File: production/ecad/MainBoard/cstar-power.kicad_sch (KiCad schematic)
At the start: 32 parts, among them IC1 LT8648SEV#PBF, U1 AZ1117IH-3.3TRG1

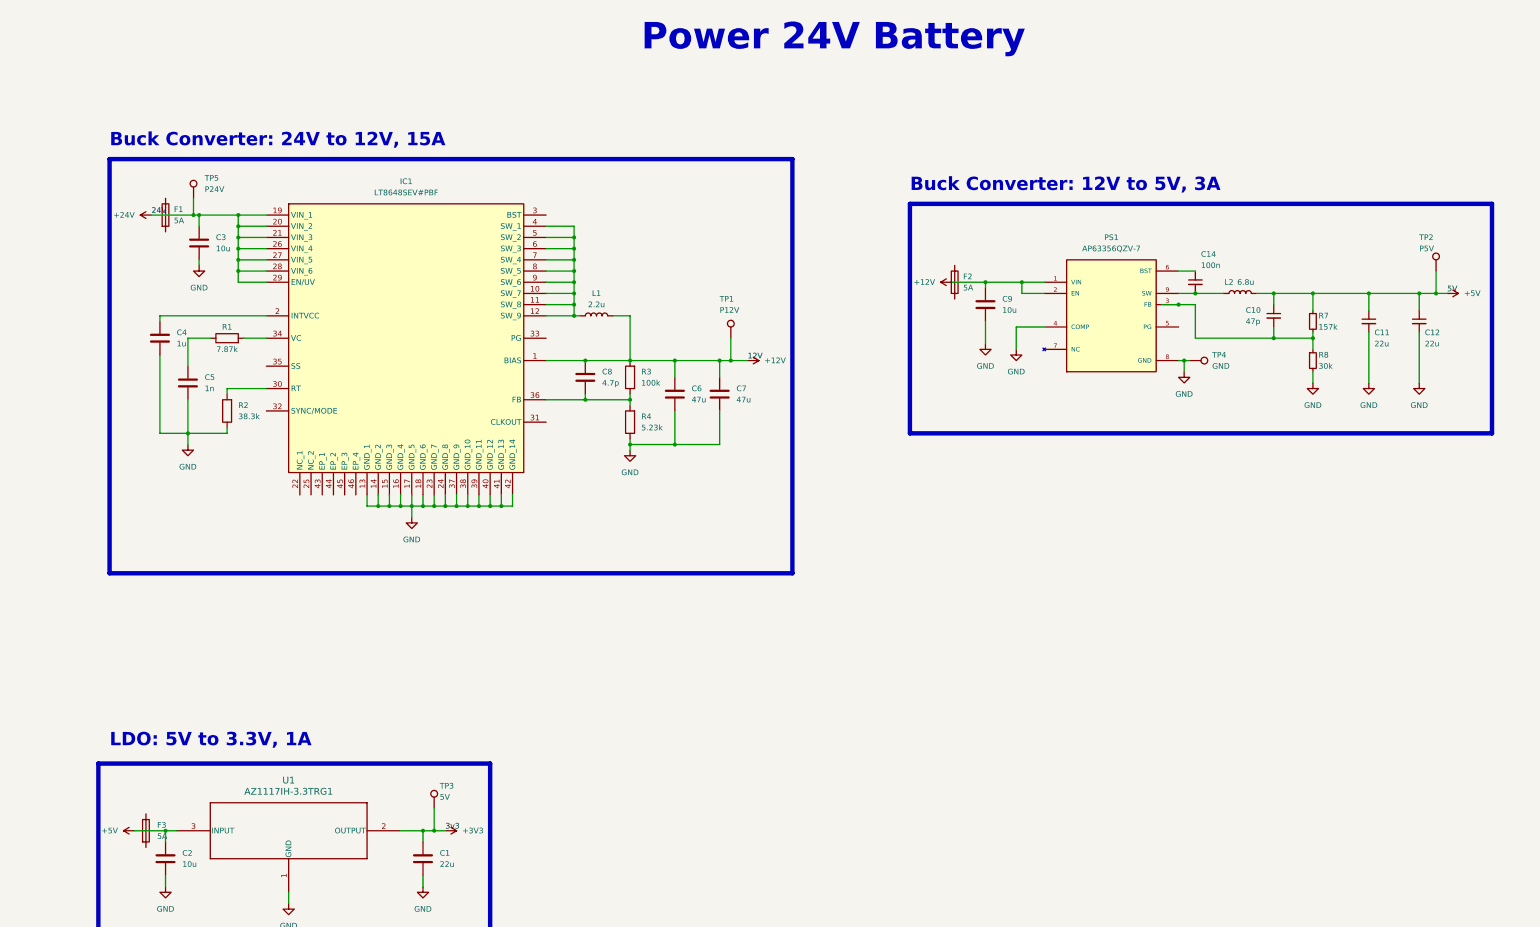
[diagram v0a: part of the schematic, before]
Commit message: Fuses position was fixed
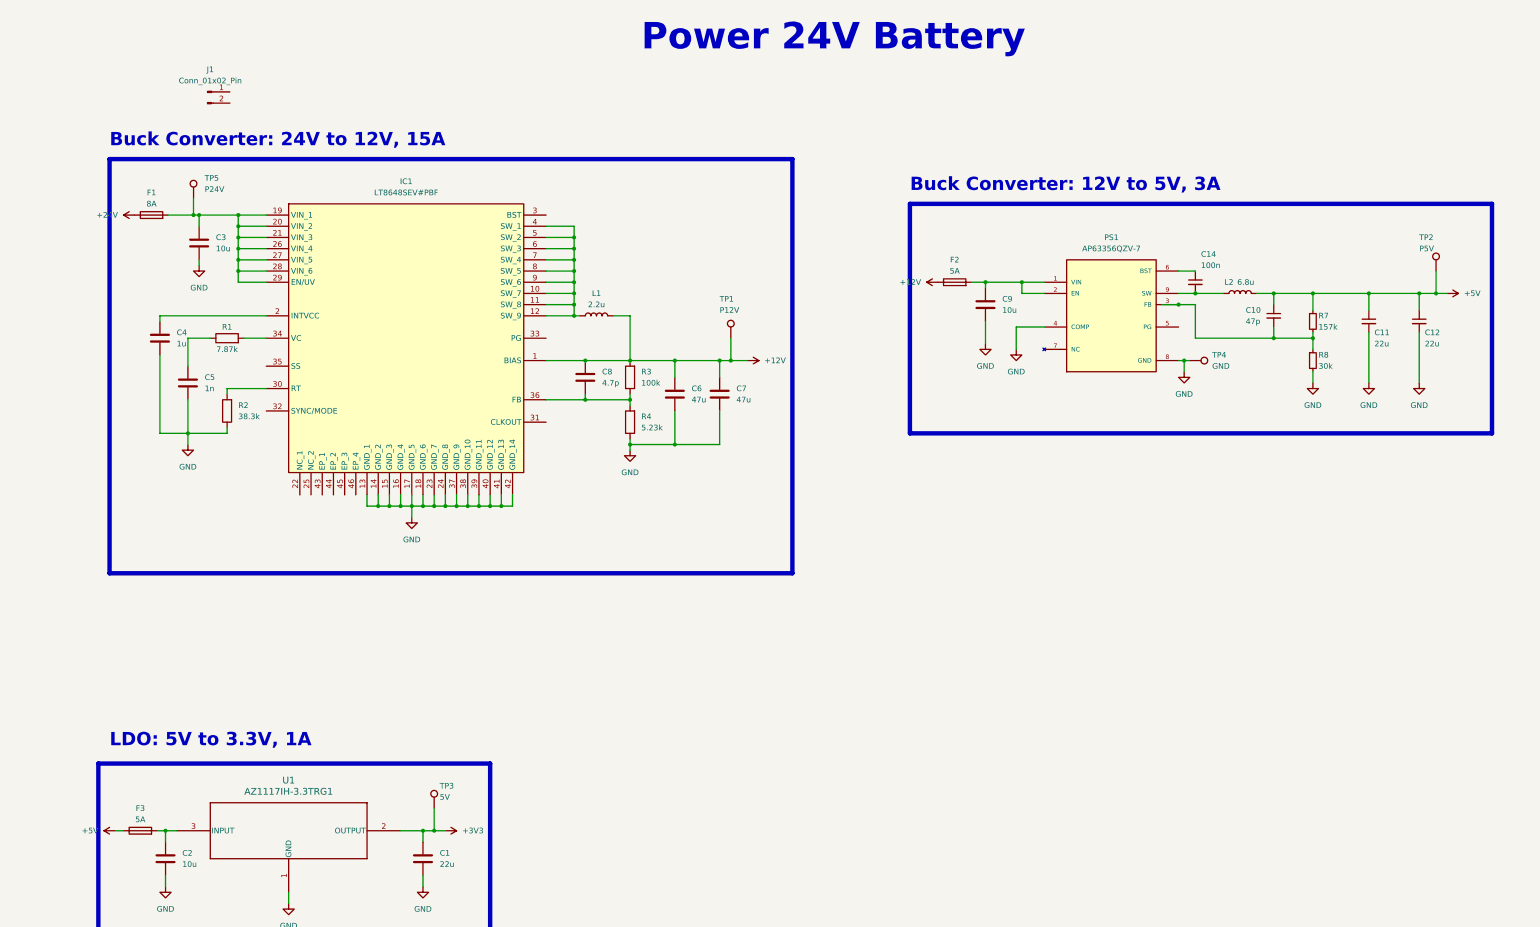
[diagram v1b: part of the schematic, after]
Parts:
- added J1: Conn_01x02_Pin, symbol Connector:Conn_01x02_Pin
- F1: value 5A -> 8A
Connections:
- net +12V: now also F2.1; no longer C9.1, PS1.1 (VIN), PS1.2 (EN)
- net +24V: now also F1.1; no longer C3.1, IC1.19 (VIN_1), IC1.20 (VIN_2), IC1.21 (VIN_3), IC1.26 (VIN_4), IC1.27 (VIN_5), IC1.28 (VIN_6), IC1.29 (EN/UV), TP5.1
- net +5V: now also F3.1; no longer C2.1, U1.3 (INPUT)
- net at F2.2: now also C9.1, PS1.1 (VIN), PS1.2 (EN)
- net at F1.2: now also C3.1, IC1.19 (VIN_1), IC1.20 (VIN_2), IC1.21 (VIN_3), IC1.26 (VIN_4), IC1.27 (VIN_5), IC1.28 (VIN_6), IC1.29 (EN/UV), TP5.1
- net at F3.2: now also C2.1, U1.3 (INPUT)
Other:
- moved on the sheet: F1, F2, F3
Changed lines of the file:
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@@
+    (stroke (width 0) (type default))
+  )
+  (wire (pts (xy 51.435 204.47) (xy 53.34 204.47))
     (stroke (width 0) (type default))
   )
@@
     (stroke (width 0) (type default))
   )
-  (wire (pts (xy 231.775 80.01) (xy 239.395 80.01))
-    (stroke (width 0) (type default))
-  )
   (wire (pts (xy 139.7 80.01) (xy 146.05 80.01))
     (stroke (width 0) (type default))
@@
     (stroke (width 0) (type default))
   )
+  (wire (pts (xy 53.975 64.77) (xy 59.69 64.77))
+    (stroke (width 0) (type default))
+  )
   (wire (pts (xy 111.76 204.47) (xy 114.3 204.47))
     (stroke (width 0) (type default))
@@
     (stroke (width 0) (type default))
   )
-  (wire (pts (xy 50.165 64.77) (xy 59.69 64.77))
-    (stroke (width 0) (type default))
-  )
   (wire (pts (xy 58.42 106.68) (xy 58.42 114.3))
     (stroke (width 0) (type default))
@@
     (stroke (width 0) (type default))
   )
-  (wire (pts (xy 46.355 204.47) (xy 53.34 204.47))
+  (wire (pts (xy 236.22 80.01) (xy 239.395 80.01))
+    (stroke (width 0) (type default))
+  )
+  (wire (pts (xy 41.91 204.47) (xy 43.815 204.47))
     (stroke (width 0) (type default))
   )
@@
     (effects (font (size 3 3) (thickness 0.6) bold) (justify left bottom))
   )
-  (label "3v3" (at 116.84 204.47 0) (fields_autoplaced)
-    (effects (font (size 1.27 1.27)) (justify left bottom))
-  )
-  (label "5V" (at 344.17 82.55 0) (fields_autoplaced)
-    (effects (font (size 1.27 1.27)) (justify left bottom))
-  )
-  (label "24V" (at 50.165 64.77 0) (fields_autoplaced)
-    (effects (font (size 1.27 1.27)) (justify left bottom))
-  )
-  (label "12V" (at 185.42 97.79 0) (fields_autoplaced)
-    (effects (font (size 1.27 1.27)) (justify left bottom))
-  )
   (symbol (lib_id "Device:C") (at 53.34 210.82 0) (unit 1)
     (in_bom yes) (on_board yes) (dnp no) (fields_autoplaced)
@@
     )
   )
-  (symbol (lib_id "power:+12V") (at 231.775 80.01 90) (unit 1)
+  (symbol (lib_id "power:+12V") (at 228.6 80.01 90) (unit 1)
     (in_bom yes) (on_board yes) (dnp no)
-    (property "Reference" "#PWR019" (at 235.585 80.01 0)
-      (effects (font (size 1.27 1.27)) hide)
-    )
-    (property "Value" "+12V" (at 227.965 80.01 90)
-      (effects (font (size 1.27 1.27)) (justify left))
-    )
-    (property "Footprint" "" (at 231.775 80.01 0)
-      (effects (font (size 1.27 1.27)) hide)
-    )
-    (property "Datasheet" "" (at 231.775 80.01 0)
+    (property "Reference" "#PWR019" (at 232.41 80.01 0)
+      (effects (font (size 1.27 1.27)) hide)
+    )
+    (property "Value" "+12V" (at 224.79 80.01 90)
+      (effects (font (size 1.27 1.27)) (justify left))
+    )
+    (property "Footprint" "" (at 228.6 80.01 0)
+      (effects (font (size 1.27 1.27)) hide)
+    )
+    (property "Datasheet" "" (at 228.6 80.01 0)
       (effects (font (size 1.27 1.27)) hide)
     )
@@
     )
   )
+  (symbol (lib_id "Connector:Conn_01x02_Pin") (at 62.865 36.83 0) (unit 1)
+    (in_bom yes) (on_board yes) (dnp no) (fields_autoplaced)
+    (property "Reference" "J1" (at 63.5 31.75 0)
+      (effects (font (size 1.27 1.27)))
+    )
+    (property "Value" "Conn_01x02_Pin" (at 63.5 34.29 0)
+      (effects (font (size 1.27 1.27)))
+    )
+    (property "Footprint" "" (at 62.865 36.83 0)
+      (effects (font (size 1.27 1.27)) hide)
+    )
+    (property "Datasheet" "~" (at 62.865 36.83 0)
+      (effects (font (size 1.27 1.27)) hide)
+    )
+    (pin "1")
+    (pin "2")
+    (instances
+      (project "cstar-power"
+        (path "/7edd775e-47a6-46f9-8e16-808bdf3a0e15"
+          (reference "J1") (unit 1)
+        )
+      )
+    )
+  )
   (symbol (lib_id "power:GND") (at 239.395 93.98 0) (unit 1)
     (in_bom yes) (on_board yes) (dnp no) (fields_autoplaced)
@@
     )
   )
-  (symbol (lib_id "Device:Fuse") (at 232.41 80.01 0) (unit 1)
-    (in_bom yes) (on_board yes) (dnp no) (fields_autoplaced)
-    (property "Reference" "F2" (at 234.315 78.74 0)
-      (effects (font (size 1.27 1.27)) (justify left))
-    )
-    (property "Value" "5A" (at 234.315 81.28 0)
-      (effects (font (size 1.27 1.27)) (justify left))
-    )
-    (property "Footprint" "" (at 230.632 80.01 90)
+  (symbol (lib_id "Device:Fuse") (at 232.41 80.01 90) (unit 1)
+    (in_bom yes) (on_board yes) (dnp no) (fields_autoplaced)
+    (property "Reference" "F2" (at 232.41 74.93 90)
+      (effects (font (size 1.27 1.27)))
+    )
+    (property "Value" "5A" (at 232.41 77.47 90)
+      (effects (font (size 1.27 1.27)))
+    )
+    (property "Footprint" "" (at 232.41 81.788 90)
       (effects (font (size 1.27 1.27)) hide)
     )
@@
     )
   )
-  (symbol (lib_id "Device:Fuse") (at 53.34 64.77 0) (unit 1)
-    (in_bom yes) (on_board yes) (dnp no) (fields_autoplaced)
-    (property "Reference" "F1" (at 55.245 63.5 0)
-      (effects (font (size 1.27 1.27)) (justify left))
-    )
-    (property "Value" "5A" (at 55.245 66.04 0)
-      (effects (font (size 1.27 1.27)) (justify left))
-    )
-    (property "Footprint" "" (at 51.562 64.77 90)
-      (effects (font (size 1.27 1.27)) hide)
-    )
-    (property "Datasheet" "~" (at 53.34 64.77 0)
+  (symbol (lib_id "Device:Fuse") (at 50.165 64.77 90) (unit 1)
+    (in_bom yes) (on_board yes) (dnp no) (fields_autoplaced)
+    (property "Reference" "F1" (at 50.165 59.69 90)
+      (effects (font (size 1.27 1.27)))
+    )
+    (property "Value" "8A" (at 50.165 62.23 90)
+      (effects (font (size 1.27 1.27)))
+    )
+    (property "Footprint" "" (at 50.165 66.548 90)
+      (effects (font (size 1.27 1.27)) hide)
+    )
+    (property "Datasheet" "~" (at 50.165 64.77 0)
       (effects (font (size 1.27 1.27)) hide)
     )
@@
     )
   )
-  (symbol (lib_id "power:+5V") (at 46.355 204.47 90) (unit 1)
-    (in_bom yes) (on_board yes) (dnp no) (fields_autoplaced)
-    (property "Reference" "#PWR015" (at 50.165 204.47 0)
-      (effects (font (size 1.27 1.27)) hide)
-    )
-    (property "Value" "+5V" (at 42.545 204.47 90)
-      (effects (font (size 1.27 1.27)) (justify left))
-    )
-    (property "Footprint" "" (at 46.355 204.47 0)
-      (effects (font (size 1.27 1.27)) hide)
-    )
-    (property "Datasheet" "" (at 46.355 204.47 0)
+  (symbol (lib_id "power:+5V") (at 41.91 204.47 90) (unit 1)
+    (in_bom yes) (on_board yes) (dnp no) (fields_autoplaced)
+    (property "Reference" "#PWR015" (at 45.72 204.47 0)
+      (effects (font (size 1.27 1.27)) hide)
+    )
+    (property "Value" "+5V" (at 38.1 204.47 90)
+      (effects (font (size 1.27 1.27)) (justify left))
+    )
+    (property "Footprint" "" (at 41.91 204.47 0)
+      (effects (font (size 1.27 1.27)) hide)
+    )
+    (property "Datasheet" "" (at 41.91 204.47 0)
       (effects (font (size 1.27 1.27)) hide)
     )
@@
     )
   )
-  (symbol (lib_id "power:+24V") (at 50.165 64.77 90) (unit 1)
-    (in_bom yes) (on_board yes) (dnp no) (fields_autoplaced)
-    (property "Reference" "#PWR017" (at 53.975 64.77 0)
-      (effects (font (size 1.27 1.27)) hide)
-    )
-    (property "Value" "+24V" (at 46.355 64.77 90)
-      (effects (font (size 1.27 1.27)) (justify left))
-    )
-    (property "Footprint" "" (at 50.165 64.77 0)
-      (effects (font (size 1.27 1.27)) hide)
-    )
-    (property "Datasheet" "" (at 50.165 64.77 0)
+  (symbol (lib_id "power:+24V") (at 46.355 64.77 90) (unit 1)
+    (in_bom yes) (on_board yes) (dnp no) (fields_autoplaced)
+    (property "Reference" "#PWR017" (at 50.165 64.77 0)
+      (effects (font (size 1.27 1.27)) hide)
+    )
+    (property "Value" "+24V" (at 42.545 64.77 90)
+      (effects (font (size 1.27 1.27)) (justify left))
+    )
+    (property "Footprint" "" (at 46.355 64.77 0)
+      (effects (font (size 1.27 1.27)) hide)
+    )
+    (property "Datasheet" "" (at 46.355 64.77 0)
       (effects (font (size 1.27 1.27)) hide)
     )
@@
     )
   )
-  (symbol (lib_id "Device:Fuse") (at 48.895 204.47 0) (unit 1)
-    (in_bom yes) (on_board yes) (dnp no) (fields_autoplaced)
-    (property "Reference" "F3" (at 51.435 203.2 0)
-      (effects (font (size 1.27 1.27)) (justify left))
-    )
-    (property "Value" "5A" (at 51.435 205.74 0)
-      (effects (font (size 1.27 1.27)) (justify left))
-    )
-    (property "Footprint" "" (at 47.117 204.47 90)
-      (effects (font (size 1.27 1.27)) hide)
-    )
-    (property "Datasheet" "~" (at 48.895 204.47 0)
-      (effects (font (size 1.27 1.27)) hide)
-    )
+  (symbol (lib_id "Device:Fuse") (at 47.625 204.47 90) (unit 1)
+    (in_bom yes) (on_board yes) (dnp no)
+    (property "Reference" "F3" (at 47.625 199.39 90)
+      (effects (font (size 1.27 1.27)))
+    )
+    (property "Value" "5A" (at 47.625 201.93 90)
+      (effects (font (size 1.27 1.27)))
+    )
+    (property "Footprint" "" (at 47.625 206.248 90)
+      (effects (font (size 1.27 1.27)) hide)
+    )
+    (property "Datasheet" "~" (at 47.625 204.47 0)
+      (effects (font (size 1.27 1.27)) hide)
+    )

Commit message: Jumpers were added to connect all 3 power rails.
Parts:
- added J2, J3: Conn_01x02_Pin, symbol Connector:Conn_01x02_Pin
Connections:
- net at C2.1, U1.3 (INPUT): now also J3.1 (Pin_1); no longer F3.2
- net at C9.1, PS1.1 (VIN), PS1.2 (EN): now also J2.1 (Pin_1); no longer F2.2
- net at J1.1 (Pin_1): now also C3.1, IC1.19 (VIN_1), IC1.20 (VIN_2), IC1.21 (VIN_3), IC1.26 (VIN_4), IC1.27 (VIN_5), IC1.28 (VIN_6), IC1.29 (EN/UV), TP5.1
- net at J1.2 (Pin_2): now also F1.2
- new net: F3.2, J3.2 (Pin_2)
- new net: F2.2, J2.2 (Pin_2)
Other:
- moved on the sheet: C1, C10, C11, C12, C14, C2, C9, F1, F2, F3, J1, L2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

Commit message: Added battery connector
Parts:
- added J4: XT60PW-M, XT60PW-M:AMASS_XT60PW-M, symbol XT60PW-M:XT60PW-M
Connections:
- net GND: now also J4.2 (-)
- new net BATT_IN: J4.1 (+)
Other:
- note added: "Battery Connector"
- moved on the sheet: C10, C11, C12, C14, C3, C4, C5, C6, C7, C8, C9, F1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

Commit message: Added TVS Diode, NC flags, diode to i/o, LEDs to each power rail
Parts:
- added D1: SMCJ26CA, SMCJ26CA:DIOM7959X262N, symbol SMCJ26CA:SMCJ26CA
- added LED1, LED2, LED3, LED4: 150080VS75000, LED_0VS75000_WRE, symbol 2024-02-25_19-51-49:150080VS75000
- added R10: 4.4k, symbol Device:R_Small
- added R5: 2k, symbol Device:R_Small
- added R6: 600, symbol Device:R_Small
- added R9: 260, symbol Device:R_Small
- TP3: value 5V -> P3V3
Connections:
- net +3V3: now also R9.1
- net GND: now also D1.1, LED1.1, LED2.1, LED3.1, LED4.1
- net at C2.1, J3.1 (Pin_1), U1.3 (INPUT): now also R6.1
- net at C9.1, J2.1 (Pin_1), PS1.1 (VIN)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: now also R5.1
- net at C3.1, IC1.19 (VIN_1), IC1.20 (VIN_2)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: now also D1.2, R10.1
- new net: LED1.2, R5.2
- new net: LED2.2, R6.2
- new net: LED4.2, R10.2
- new net: LED3.2, R9.2
- no-connect marks 0 -> 6
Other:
- note added: "Bidirectional TVS Diode"
- note added: "Green LED"
- note added: "Protection Circutry: Three 5A Protection Fuses to the 12V, 5V, and 3v3 power rails. TVS Diode"
- note removed: "Protection Circutry: Three 5A Circuit Protection Fuses were added to the 12V, 5V, and 3v3 power rails."
- moved on the sheet: C1, C10, C11, C12, C14, C2, C3, C4, C5, C6, C7, C8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

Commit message: added note
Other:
- note added: "Add large resistors for LEDs for proper power dissipation in layout"
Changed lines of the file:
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@@
+    (effects (font (size 3 3) (thickness 0.6) bold) (justify left bottom))
+  )
+  (text "Add large resistors for LEDs for proper power dissipation in layout\n\n"
+    (at 24.13 274.32 0)
     (effects (font (size 3 3) (thickness 0.6) bold) (justify left bottom))
   )

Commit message: added test points
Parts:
- added TP6: P12V, symbol Connector:TestPoint
- added TP7: P5V, symbol Connector:TestPoint
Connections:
- net at C2.1, J3.1 (Pin_1), R6.1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: now also TP7.1
- net at C9.1, J2.1 (Pin_1), PS1.1 (VIN)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: now also TP6.1
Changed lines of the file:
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@@
   (junction (at 264.16 177.8) (diameter 0) (color 0 0 0 0)
   )
+  (junction (at 237.49 177.8) (diameter 0) (color 0 0 0 0)
+  )
   (junction (at 162.56 125.73) (diameter 0) (color 0 0 0 0)
   )
@@
   )
   (junction (at 199.39 111.76) (diameter 0) (color 0 0 0 0)
+  )
+  (junction (at 68.58 175.26) (diameter 0) (color 0 0 0 0)
   )
   (junction (at 157.48 125.73) (diameter 0) (color 0 0 0 0)
@@
     (stroke (width 0) (type default))
   )
-  (wire (pts (xy 64.77 175.26) (xy 72.39 175.26))
+  (wire (pts (xy 64.77 175.26) (xy 68.58 175.26))
     (stroke (width 0) (type default))
   )
@@
     (stroke (width 0) (type default))
   )
+  (wire (pts (xy 68.58 175.26) (xy 72.39 175.26))
+    (stroke (width 0) (type default))
+  )
   (wire (pts (xy 199.39 102.87) (xy 199.39 101.6))
     (stroke (width 0) (type default))
@@
     (stroke (width 0) (type default))
   )
+  (wire (pts (xy 237.49 177.8) (xy 242.57 177.8))
+    (stroke (width 0) (type default))
+  )
   (wire (pts (xy 264.16 180.34) (xy 264.16 177.8))
     (stroke (width 0) (type default))
@@
     (stroke (width 0) (type default))
   )
+  (wire (pts (xy 237.49 175.26) (xy 237.49 177.8))
+    (stroke (width 0) (type default))
+  )
   (wire (pts (xy 199.39 100.33) (xy 199.39 101.6))
     (stroke (width 0) (type default))
@@
     (stroke (width 0) (type default))
   )
-  (wire (pts (xy 232.41 177.8) (xy 242.57 177.8))
+  (wire (pts (xy 68.58 172.72) (xy 68.58 175.26))
+    (stroke (width 0) (type default))
+  )
+  (wire (pts (xy 232.41 177.8) (xy 237.49 177.8))
     (stroke (width 0) (type default))
   )
@@
   (symbol (lib_id "Connector:Conn_01x02_Pin") (at 64.77 170.18 270) (unit 1)
     (in_bom yes) (on_board yes) (dnp no)
-    (property "Reference" "J3" (at 57.15 165.1 90)
-      (effects (font (size 1.27 1.27)) (justify left))
-    )
-    (property "Value" "Conn_01x02_Pin" (at 57.15 167.64 90)
+    (property "Reference" "J3" (at 52.07 179.07 90)
+      (effects (font (size 1.27 1.27)) (justify left))
+    )
+    (property "Value" "Conn_01x02_Pin" (at 52.07 181.61 90)
       (effects (font (size 1.27 1.27)) (justify left))
     )
@@
     )
   )
+  (symbol (lib_id "Connector:TestPoint") (at 68.58 172.72 0) (unit 1)
+    (in_bom yes) (on_board yes) (dnp no)
+    (property "Reference" "TP7" (at 67.31 165.1 0)
+      (effects (font (size 1.27 1.27)) (justify left))
+    )
+    (property "Value" "P5V" (at 67.31 167.64 0)
+      (effects (font (size 1.27 1.27)) (justify left))
+    )
+    (property "Footprint" "" (at 73.66 172.72 0)
+      (effects (font (size 1.27 1.27)) hide)
+    )
+    (property "Datasheet" "~" (at 73.66 172.72 0)
+      (effects (font (size 1.27 1.27)) hide)
+    )
+    (pin "1")
+    (instances
+      (project "cstar-power"
+        (path "/7edd775e-47a6-46f9-8e16-808bdf3a0e15"
+          (reference "TP7") (unit 1)
+        )
+      )
+    )
+  )
   (symbol (lib_id "Connector:Conn_01x02_Pin") (at 232.41 172.72 270) (unit 1)
-    (in_bom yes) (on_board yes) (dnp no) (fields_autoplaced)
-    (property "Reference" "J2" (at 234.315 172.085 90)
-      (effects (font (size 1.27 1.27)) (justify left))
-    )
-    (property "Value" "Conn_01x02_Pin" (at 234.315 174.625 90)
+    (in_bom yes) (on_board yes) (dnp no)
+    (property "Reference" "J2" (at 223.52 181.61 90)
+      (effects (font (size 1.27 1.27)) (justify left))
+    )
+    (property "Value" "Conn_01x02_Pin" (at 223.52 184.15 90)
       (effects (font (size 1.27 1.27)) (justify left))
     )
@@
         )
       )
+    )
+  )
+  (symbol (lib_id "Connector:TestPoint") (at 237.49 175.26 0) (unit 1)
+    (in_bom yes) (on_board yes) (dnp no)
+    (property "Reference" "TP6" (at 234.95 166.37 0)
+      (effects (font (size 1.27 1.27)) (justify left))
+    )
+    (property "Value" "P12V" (at 234.95 168.91 0)
+      (effects (font (size 1.27 1.27)) (justify left))
+    )
+    (property "Footprint" "" (at 242.57 175.26 0)
+      (effects (font (size 1.27 1.27)) hide)
+    )
+    (property "Datasheet" "~" (at 242.57 175.26 0)
+      (effects (font (size 1.27 1.27)) hide)
+    )
+    (pin "1")
+    (instances
+      (project "cstar-power"
+        (path "/7edd775e-47a6-46f9-8e16-808bdf3a0e15"
+          (reference "TP6") (unit 1)
+        )
+      )
